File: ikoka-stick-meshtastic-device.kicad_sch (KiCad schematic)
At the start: 26 parts, among them J1 Conn_Coaxial, J2 Conn_01x07_Socket, J3 Conn_01x07_Socket, J4 Conn_01x02, J5 Conn_01x02, J6 Conn_01x04, Q1 AO3401A, SW1 SW_Push, U1 MT3608, U2 E22-900M30S, U3 XIAO-ESP32-S3-SMD

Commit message: feat: Replace MT3608 boost with XL3608 commercial module footprint
Remove U1, L1, D1, R1, R2, C3, C4 and add PS1 (4 solder pads, assumed
24.4x13.7mm + 10% margin, to be updated with caliper measurements).
Schematic also saved in KiCad 10 format.

Co-Authored-By: Claude Sonnet 5.5 <noreply@anthropic.com>
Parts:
- removed C3, C4: 47uF, Capacitor_SMD:C_0805_2012Metric, symbol Device:C
- removed D1: SS34, Diode_SMD:D_SMA, symbol Device:D_Schottky
- removed L1: 22uH, Inductor_SMD:L_Sunlord_MWSA0624S, symbol Device:L
- removed R1: 300K, Resistor_SMD:R_0603_1608Metric, symbol Device:R
- removed R2: 39K, Resistor_SMD:R_0603_1608Metric, symbol Device:R
- removed U1: MT3608, Package_TO_SOT_SMD:SOT-23-6, symbol Regulator_Switching:MT3608
- added PS1: XL3608 5V Boost Module, Booster_Module:Booster_XL3608_24.4x13.7mm_Solder, symbol Connector_Generic:Conn_01x04
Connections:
- net +5V2_LORA: now also PS1.4 (Pin_4)
- net BOOST_IN: now also PS1.1 (Pin_1)
- net GND: now also PS1.2 (Pin_2), PS1.3 (Pin_3)

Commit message: fix: Route PS1, sync PCB nets from schematic and clean up DRC
- Update J3.5, J6.3, J6.4 pad nets to match schematic (+3V3, /I2C_SCL, /I2C_SDA)
- Rotate PS1 header 180 deg in place so BOOST_IN lands in its pour; route
  PS1.4 to the +5V2_LORA pour with a 0.6 mm F.Cu track
- Remove leftover no-net zone and orphan GND vias from the old booster; refill zones
- Include PS1 in BOM to match the symbol
- Use ${KIPRJMOD} for the Booster_Module footprint library path
- PCB and project saved in KiCad 10 format

DRC: 0 errors, 0 unconnected, 0 parity issues.

Co-Authored-By: Claude Opus 5.5 <noreply@anthropic.com>
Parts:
- PS1: value XL3608 5V Boost Module -> XL3608 5V Boost (wired); footprint Booster_Module:Booster_XL3608_24.4x13.7mm_Solder -> Connector_PinHeader_2.54mm:PinHeader_2x02_P2.54mm_Vertical
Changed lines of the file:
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@@
 	)
 	(label "BOOST_IN"
+		(at 40.64 35.56 180)
+		(effects
+			(font
+				(size 1.27 1.27)
+			)
+			(justify right bottom)
+		)
+	)
+	(label "BOOST_IN"
 		(at 17.78 25.4 0)
 		(effects
@@
 		)
 	)
+	(label "GND"
+		(at 40.64 38.1 180)
+		(effects
+			(font
+				(size 1.27 1.27)
+			)
+			(justify right bottom)
+		)
+	)
 	(label "LORA_RXEN"
 		(at 172.72 54.61 0)
@@
 		)
 	)
+	(label "+5V2_LORA"
+		(at 40.64 43.18 180)
+		(effects
+			(font
+				(size 1.27 1.27)
+			)
+			(justify right bottom)
+		)
+	)
 	(label "LORA_RXEN"
 		(at 53.34 170.18 0)
@@
 		)
 	)
+	(label "GND"
+		(at 40.64 40.64 180)
+		(effects
+			(font
+				(size 1.27 1.27)
+			)
+			(justify right bottom)
+		)
+	)
 	(label "D0"
 		(at 53.34 157.48 0)
@@
 		(exclude_from_sim no)
 		(in_bom yes)
-		(on_board no)
-		(in_pos_files no)
+		(on_board yes)
+		(in_pos_files yes)
 		(dnp no)
 		(property "Reference" "J3"
@@
 		(exclude_from_sim no)
 		(in_bom yes)
-		(on_board no)
-		(in_pos_files no)
+		(on_board yes)
+		(in_pos_files yes)
 		(dnp no)
 		(fields_autoplaced yes)
@@
 	)
 	(symbol
+		(lib_id "Connector_Generic:Conn_01x04")
+		(at 45.72 38.1 0)
+		(unit 1)
+		(body_style 1)
+		(exclude_from_sim no)
+		(in_bom yes)
+		(on_board yes)
+		(in_pos_files yes)
+		(dnp no)
+		(property "Reference" "PS1"
+			(at 45.72 43.18 0)
+			(show_name no)
+			(do_not_autoplace no)
+			(effects
+				(font
+					(size 1.27 1.27)
+				)
+			)
+		)
+		(property "Value" "XL3608 5V Boost (wired)"
+			(at 45.72 30.48 0)
+			(show_name no)
+			(do_not_autoplace no)
+			(effects
+				(font
+					(size 1.27 1.27)
+				)
+			)
+		)
+		(property "Footprint" "Connector_PinHeader_2.54mm:PinHeader_2x02_P2.54mm_Vertical"
+			(at 45.72 38.1 0)
+			(hide yes)
+			(show_name no)
+			(do_not_autoplace no)
+			(effects
+				(font
+					(size 1.27 1.27)
+				)
+			)
+		)
+		(property "Datasheet" ""
+			(at 45.72 38.1 0)
+			(hide yes)
+			(show_name no)
+			(do_not_autoplace no)
+			(effects
+				(font
+					(size 1.27 1.27)
+				)
+			)
+		)
+		(property "Description" "Generic connector, single row, 01x04, script generated (kicad-library-utils/schlib/autogen/connector/)"
+			(at 45.72 38.1 0)
+			(hide yes)
+			(show_name no)
+			(do_not_autoplace no)
+			(effects
+				(font
+					(size 1.27 1.27)
+				)
+			)
+		)
+		(pin "1"
+		)
+		(pin "2"
+		)
+		(pin "3"
+		)
+		(pin "4"
+		)
+		(instances
+			(project "ikoka-stick-meshtastic-device"
+				(path "/d817f34c-2aa5-4c70-878b-29719eb987fe"
+					(reference "PS1")
+					(unit 1)
+				)
+			)
+		)
+	)
+	(symbol
 		(lib_id "power:PWR_FLAG")
 		(at 191.77 107.95 0)
@@
 		(exclude_from_sim no)
 		(in_bom yes)
-		(on_board no)
-		(in_pos_files no)
+		(on_board yes)
+		(in_pos_files yes)
 		(dnp no)
 		(fields_autoplaced yes)
@@
 		)
 	)
-	(symbol
-		(lib_id "Connector_Generic:Conn_01x04")
-		(at 45.72 38.1 0)
-		(unit 1)
-		(body_style 1)
-		(exclude_from_sim no)
-		(in_bom yes)
-		(on_board yes)
-		(in_pos_files yes)
-		(dnp no)
-		(property "Reference" "PS1"
-			(at 45.72 43.18 0)
-			(show_name no)
-			(do_not_autoplace no)
-			(effects
-				(font
-					(size 1.27 1.27)
-				)
-			)
-		)
-		(property "Value" "XL3608 5V Boost Module"
-			(at 45.72 30.48 0)
-			(show_name no)
-			(do_not_autoplace no)
-			(effects
-				(font
-					(size 1.27 1.27)
-				)
-			)
-		)
-		(property "Footprint" "Booster_Module:Booster_XL3608_24.4x13.7mm_Solder"
-			(at 45.72 38.1 0)
-			(hide yes)
-			(show_name no)
-			(do_not_autoplace no)
-			(effects
-				(font
-					(size 1.27 1.27)
-				)
-			)
-		)
-		(property "Datasheet" ""
-			(at 45.72 38.1 0)
-			(hide yes)
-			(show_name no)
-			(do_not_autoplace no)
-			(effects
-				(font
-					(size 1.27 1.27)
-				)
-			)
-		)
-		(property "Description" "Generic connector, single row, 01x04, script generated (kicad-library-utils/schlib/autogen/connector/)"
-			(at 45.72 38.1 0)
-			(hide yes)
-			(show_name no)
-			(do_not_autoplace no)
-			(effects
-				(font
-					(size 1.27 1.27)
-				)
-			)
-		)
-		(pin "1"
-		)
-		(pin "2"
-		)
-		(pin "3"
-		)
-		(pin "4"
-		)
-		(instances
-			(project "ikoka-stick-meshtastic-device"
-				(path "/d817f34c-2aa5-4c70-878b-29719eb987fe"
-					(reference "PS1")
-					(unit 1)
-				)
-			)
-		)
-	)
-	(label "BOOST_IN"
-		(at 40.64 35.56 180)
-		(effects
-			(font
-				(size 1.27 1.27)
-			)
-			(justify right bottom)
-		)
-	)
-	(label "GND"
-		(at 40.64 38.1 180)
-		(effects
-			(font
-				(size 1.27 1.27)
-			)
-			(justify right bottom)
-		)
-	)
-	(label "GND"
-		(at 40.64 40.64 180)
-		(effects
-			(font
-				(size 1.27 1.27)
-			)
-			(justify right bottom)
-		)
-	)
-	(label "+5V2_LORA"
-		(at 40.64 43.18 180)
-		(effects
-			(font
-				(size 1.27 1.27)
-			)
-			(justify right bottom)
-		)
-	)
-	(junction
-		(at 223.52 34.29)
-		(diameter 0)
-		(color 0 0 0 0)
-	)
-	(junction
-		(at 223.52 59.69)
-		(diameter 0)
-		(color 0 0 0 0)
-	)
 	(sheet_instances

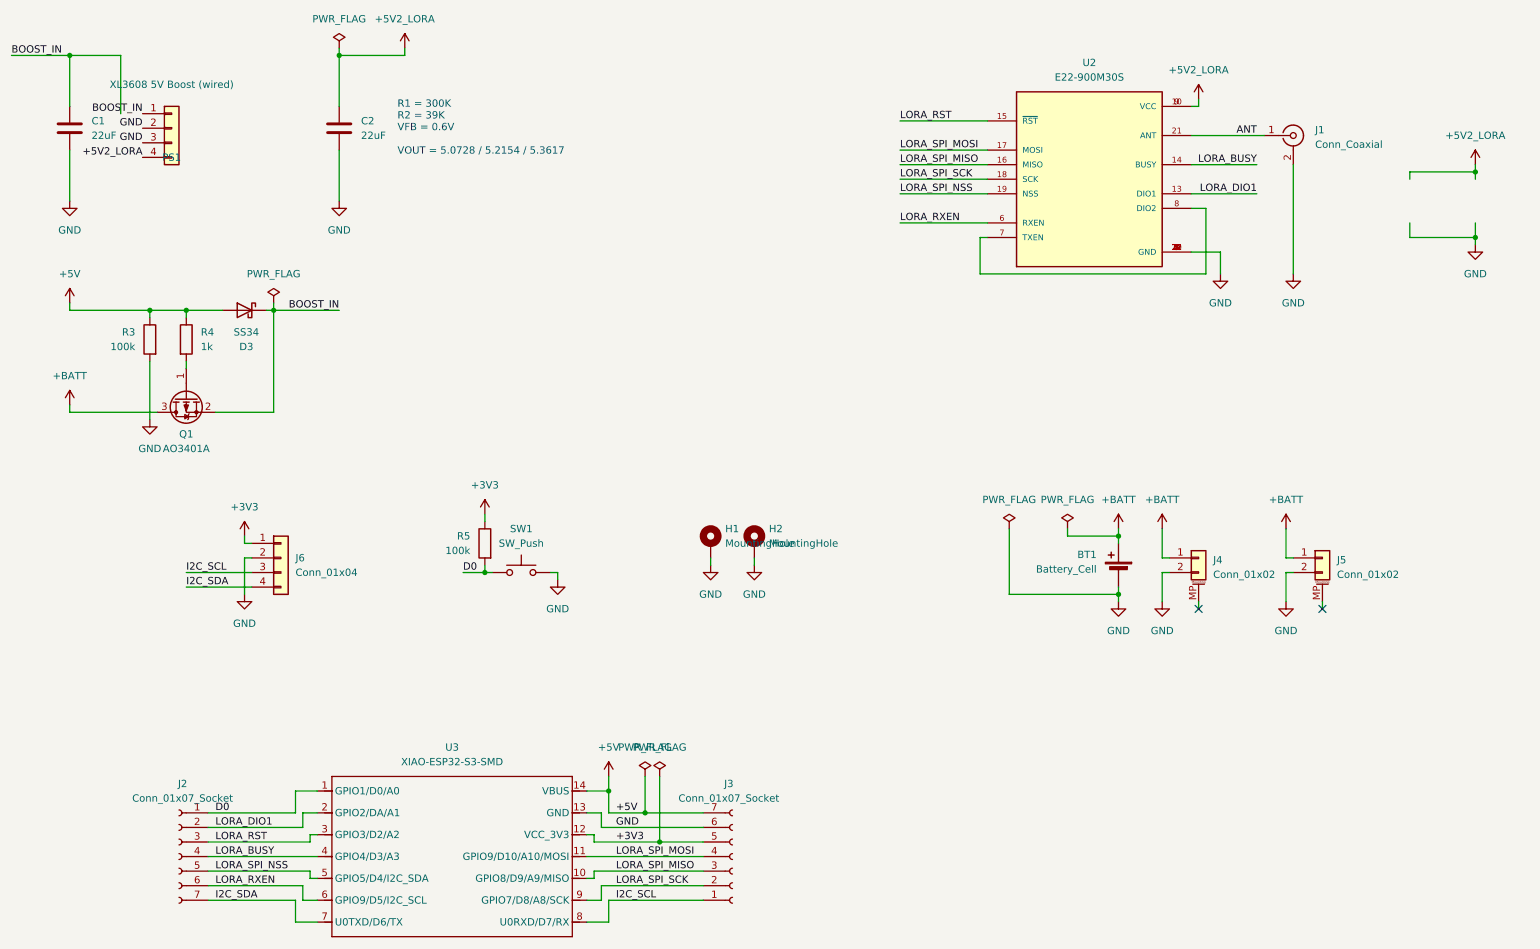
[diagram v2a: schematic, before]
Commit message: feat: v2 - drop 21700 battery, mount XL3608 module on the back
- Remove BT1 (21700 holder) and its B.Cu +BATT pours/vias; trim the F.Cu
  +BATT strip to J5. Board is powered from the XIAO USB 5V.
- Keep D3 (VBUS backfeed block), C1, and the Q1/R3/R4 power path with
  J4/J5 for an optional LiPo; rejoin Q1-J4-J5 with a back track.
- New footprint Booster_XL3608_24.4x13.7mm_SMD (SMD pads only, assumed
  positions, VIN/VOUT/GND silk labels). PS1 placed on B.Cu, vertical, under
  the old header spot, clear of the E22 RF area. Only its own pads are
  exposed under the module (vias tented).
- Silkscreen HW Ver. 2.0.0; README power section updated.

DRC: 0 errors, 0 unconnected, 0 parity issues.

Co-Authored-By: Claude Opus 5.5 <noreply@anthropic.com>
Claude-Session: https://claude.ai/code/session_013aihWTyEvMfq2tmgNbS7qs
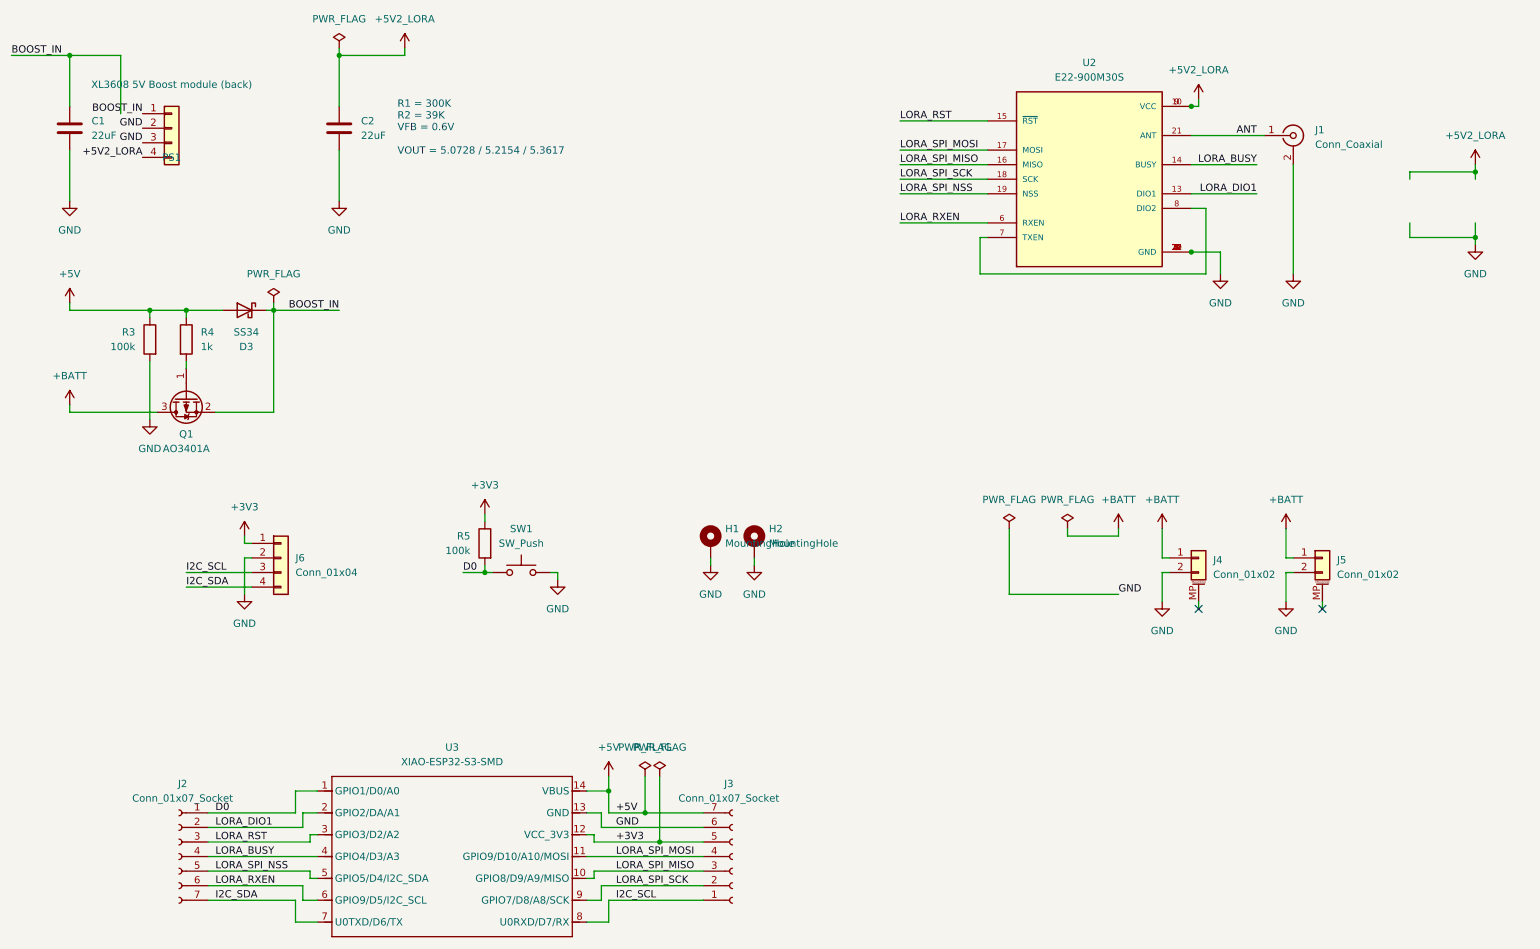
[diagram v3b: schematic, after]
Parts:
- removed BT1: Battery_Cell, Battery 21700:BatteryHolder_MYOUNG_BH-21700-B1BJ001_1x21700, symbol Device:Battery_Cell
- PS1: value XL3608 5V Boost (wired) -> XL3608 5V Boost module (back); footprint Connector_PinHeader_2.54mm:PinHeader_2x02_P2.54mm_Vertical -> Booster_Module:Booster_XL3608_24.4x13.7mm_SMD
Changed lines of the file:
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@@
 	)
 	(junction
-		(at 210.82 109.22)
-		(diameter 0)
-		(color 0 0 0 0)
-	)
-	(junction
 		(at 48.26 69.85)
 		(diameter 0)
@@
 	)
 	(junction
-		(at 210.82 119.38)
-		(diameter 0)
-		(color 0 0 0 0)
-	)
-	(junction
 		(at 74.93 25.4)
 		(diameter 0)
@@
 	(wire
 		(pts
-			(xy 210.82 109.22) (xy 210.82 110.49)
-		)
-		(stroke
-			(width 0)
-			(type default)
-		)
-	)
-	(wire
-		(pts
-			(xy 210.82 120.65) (xy 210.82 119.38)
-		)
-		(stroke
-			(width 0)
-			(type default)
-		)
-	)
-	(wire
-		(pts
 			(xy 69.85 168.91) (xy 71.12 168.91)
 		)
@@
 	(wire
 		(pts
-			(xy 210.82 118.11) (xy 210.82 119.38)
-		)
-		(stroke
-			(width 0)
-			(type default)
-		)
-	)
-	(wire
-		(pts
 			(xy 172.72 44.45) (xy 187.96 44.45)
 		)
@@
 	)
 	(symbol
-		(lib_id "Device:Battery_Cell")
-		(at 210.82 115.57 0)
-		(mirror y)
-		(unit 1)
-		(body_style 1)
-		(exclude_from_sim no)
-		(in_bom yes)
-		(on_board yes)
-		(in_pos_files yes)
-		(dnp no)
-		(property "Reference" "BT1"
-			(at 207.01 112.4584 0)
-			(show_name no)
-			(do_not_autoplace no)
-			(effects
-				(font
-					(size 1.27 1.27)
-				)
-				(justify left)
-			)
-		)
-		(property "Value" "Battery_Cell"
-			(at 207.01 114.9984 0)
-			(show_name no)
-			(do_not_autoplace no)
-			(effects
-				(font
-					(size 1.27 1.27)
-				)
-				(justify left)
-			)
-		)
-		(property "Footprint" "Battery 21700:BatteryHolder_MYOUNG_BH-21700-B1BJ001_1x21700"
-			(at 210.82 114.046 90)
-			(hide yes)
-			(show_name no)
-			(do_not_autoplace no)
-			(effects
-				(font
-					(size 1.27 1.27)
-				)
-			)
-		)
-		(property "Datasheet" ""
-			(at 210.82 114.046 90)
-			(hide yes)
-			(show_name no)
-			(do_not_autoplace no)
-			(effects
-				(font
-					(size 1.27 1.27)
-				)
-			)
-		)
-		(property "Description" "Single-cell battery"
-			(at 210.82 115.57 0)
-			(hide yes)
-			(show_name no)
-			(do_not_autoplace no)
-			(effects
-				(font
-					(size 1.27 1.27)
-				)
-			)
-		)
-		(property "LCSC" "C20606791"
-			(at 207.01 112.4584 0)
-			(hide yes)
-			(show_name no)
-			(do_not_autoplace no)
-			(effects
-				(font
-					(size 1.27 1.27)
-				)
-			)
-		)
-		(pin "1"
-		)
-		(pin "2"
-		)
-		(instances
-			(project "ikoka-stick-meshtastic-device"
-				(path "/d817f34c-2aa5-4c70-878b-29719eb987fe"
-					(reference "BT1")
-					(unit 1)
-				)
-			)
-		)
-	)
-	(symbol
 		(lib_id "Connector_Generic_MountingPin:Conn_01x02_MountingPin")
 		(at 246.38 113.03 0)
@@
 	)
 	(symbol
-		(lib_id "power:GND")
-		(at 210.82 120.65 0)
-		(unit 1)
-		(body_style 1)
-		(exclude_from_sim no)
-		(in_bom yes)
-		(on_board yes)
-		(in_pos_files yes)
-		(dnp no)
-		(fields_autoplaced yes)
-		(property "Reference" "#PWR010"
-			(at 210.82 127 0)
-			(hide yes)
-			(show_name no)
-			(do_not_autoplace no)
-			(effects
-				(font
-					(size 1.27 1.27)
-				)
-			)
-		)
-		(property "Value" "GND"
-			(at 210.82 125.73 0)
-			(show_name no)
-			(do_not_autoplace no)
-			(effects
-				(font
-					(size 1.27 1.27)
-				)
-			)
-		)
-		(property "Footprint" ""
-			(at 210.82 120.65 0)
-			(hide yes)
-			(show_name no)
-			(do_not_autoplace no)
-			(effects
-				(font
-					(size 1.27 1.27)
-				)
-			)
-		)
-		(property "Datasheet" ""
-			(at 210.82 120.65 0)
-			(hide yes)
-			(show_name no)
-			(do_not_autoplace no)
-			(effects
-				(font
-					(size 1.27 1.27)
-				)
-			)
-		)
-		(property "Description" "Power symbol creates a global label with name \"GND\" , ground"
-			(at 210.82 120.65 0)
-			(hide yes)
-			(show_name no)
-			(do_not_autoplace no)
-			(effects
-				(font
-					(size 1.27 1.27)
-				)
-			)
-		)
-		(pin "1"
-		)
-		(instances
-			(project "ikoka-stick-meshtastic-device"
-				(path "/d817f34c-2aa5-4c70-878b-29719eb987fe"
-					(reference "#PWR010")
-					(unit 1)
-				)
-			)
-		)
-	)
-	(symbol
 		(lib_id "Seeed_Studio_XIAO_Series:XIAO-ESP32-S3-DIP")
 		(at 73.66 148.59 0)
@@
 			)
 		)
-		(property "Value" "XL3608 5V Boost (wired)"
+		(property "Value" "XL3608 5V Boost module (back)"
 			(at 45.72 30.48 0)
 			(show_name no)
@@
 			)
 		)
-		(property "Footprint" "Connector_PinHeader_2.54mm:PinHeader_2x02_P2.54mm_Vertical"
+		(property "Footprint" "Booster_Module:Booster_XL3608_24.4x13.7mm_SMD"
 			(at 45.72 38.1 0)
 			(hide yes)
@@
 		)
 	)
+	(junction
+		(at 223.52 34.29)
+		(diameter 0)
+		(color 0 0 0 0)
+	)
+	(junction
+		(at 223.52 59.69)
+		(diameter 0)
+		(color 0 0 0 0)
+	)
+	(label "GND"
+		(at 210.82 119.38 0)
+		(effects
+			(font
+				(size 1.27 1.27)
+			)
+			(justify left bottom)
+		)
+	)

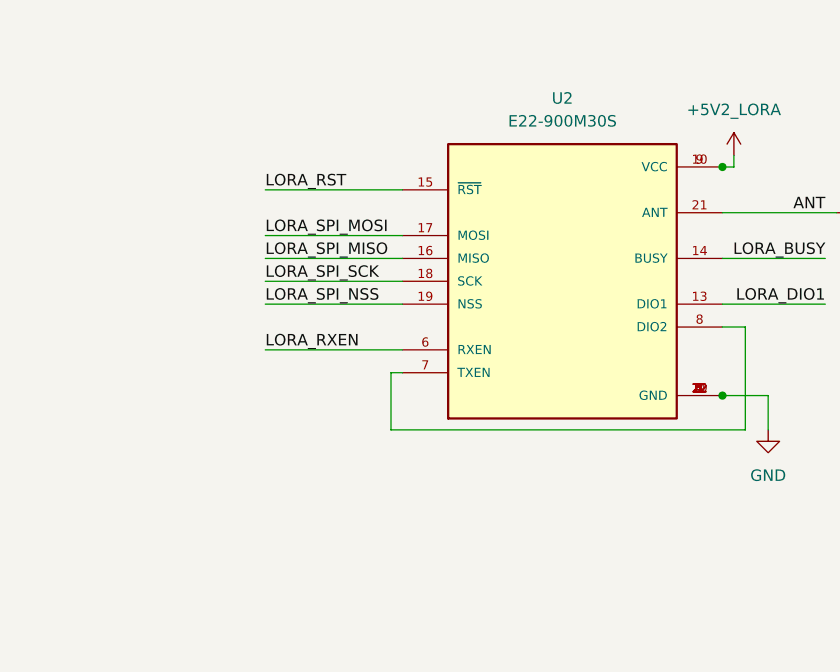
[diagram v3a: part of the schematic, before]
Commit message: feat: v3 - use E22P LoRa module (EN jumper JP1), ported from tahnok fork
E22P pin 6 is EN (must be high) instead of RXEN: route it to solder
jumper JP1 under the XIAO, bridged to 3V3 by default, D6 optional.
Pin 7 (T/R CTRL) stays on DIO2. Symbol and routing from
tahnok/ikoka-stick-meshtastic-device 366648b.

Co-Authored-By: Claude Opus 5.5 <noreply@anthropic.com>
Claude-Session: https://claude.ai/code/session_013aihWTyEvMfq2tmgNbS7qs
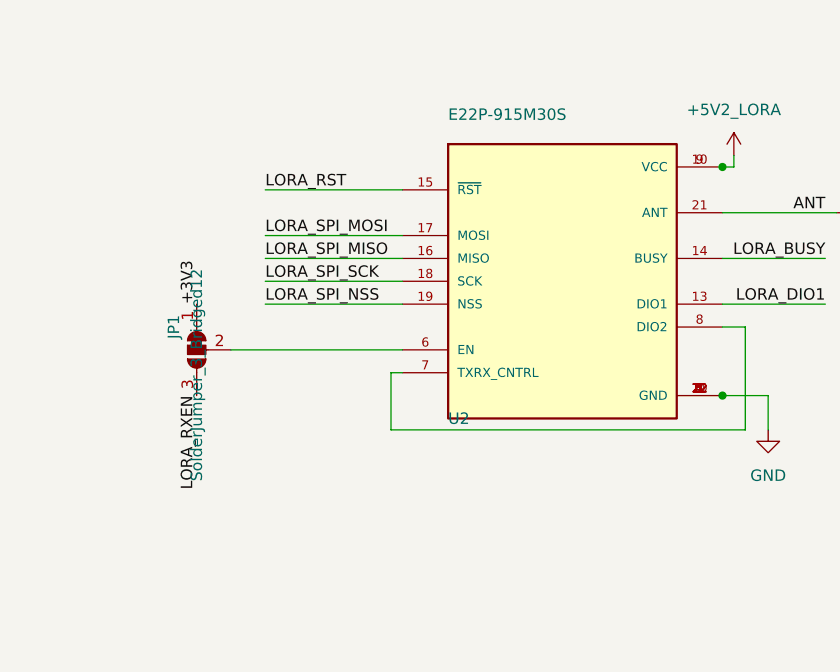
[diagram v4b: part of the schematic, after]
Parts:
- removed U2: E22-900M30S, E22-900M30S:XCVR_E22-900M30S, symbol E22-900M30S:E22-900M30S
- added JP1: SolderJumper_3_Bridged12, Jumper:SolderJumper-3_P1.3mm_Bridged12_RoundedPad1.0x1.5mm_NumberLabels, symbol Jumper:SolderJumper_3_Bridged12
- added U2: E22P-915M30S, E22-900M30S:XCVR_E22-900M30S, symbol E22-900M30S:E22P-915M30S
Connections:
- net +3V3: now also JP1.1 (A)
- net +5V2_LORA: now also U2.10 (VCC), U2.9 (VCC)
- net ANT: now also U2.21 (ANT)
- net GND: now also U2.1 (GND), U2.11 (GND), U2.12 (GND), U2.2 (GND), U2.20 (GND), U2.22 (GND), U2.3 (GND), U2.4 (GND), U2.5 (GND)
- net LORA_BUSY: now also U2.14 (BUSY)
- net LORA_DIO1: now also U2.13 (DIO1)
- net LORA_RST: now also U2.15 (~{RST})
- net LORA_RXEN: now also JP1.3 (B)
- net LORA_SPI_MISO: now also U2.16 (MISO)
- net LORA_SPI_MOSI: now also U2.17 (MOSI)
- net LORA_SPI_NSS: now also U2.19 (NSS)
- net LORA_SPI_SCK: now also U2.18 (SCK)
- new net: JP1.2 (C), U2.6 (EN)
- new net: U2.7 (TXRX_CNTRL), U2.8 (DIO2)
